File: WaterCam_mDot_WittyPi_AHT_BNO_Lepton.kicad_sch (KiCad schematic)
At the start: 9 parts, among them J1 GPIO, J2 FLIR Lepton Socket, J6 Witty Pi 4 7-Pin Header, Q1 NMOS

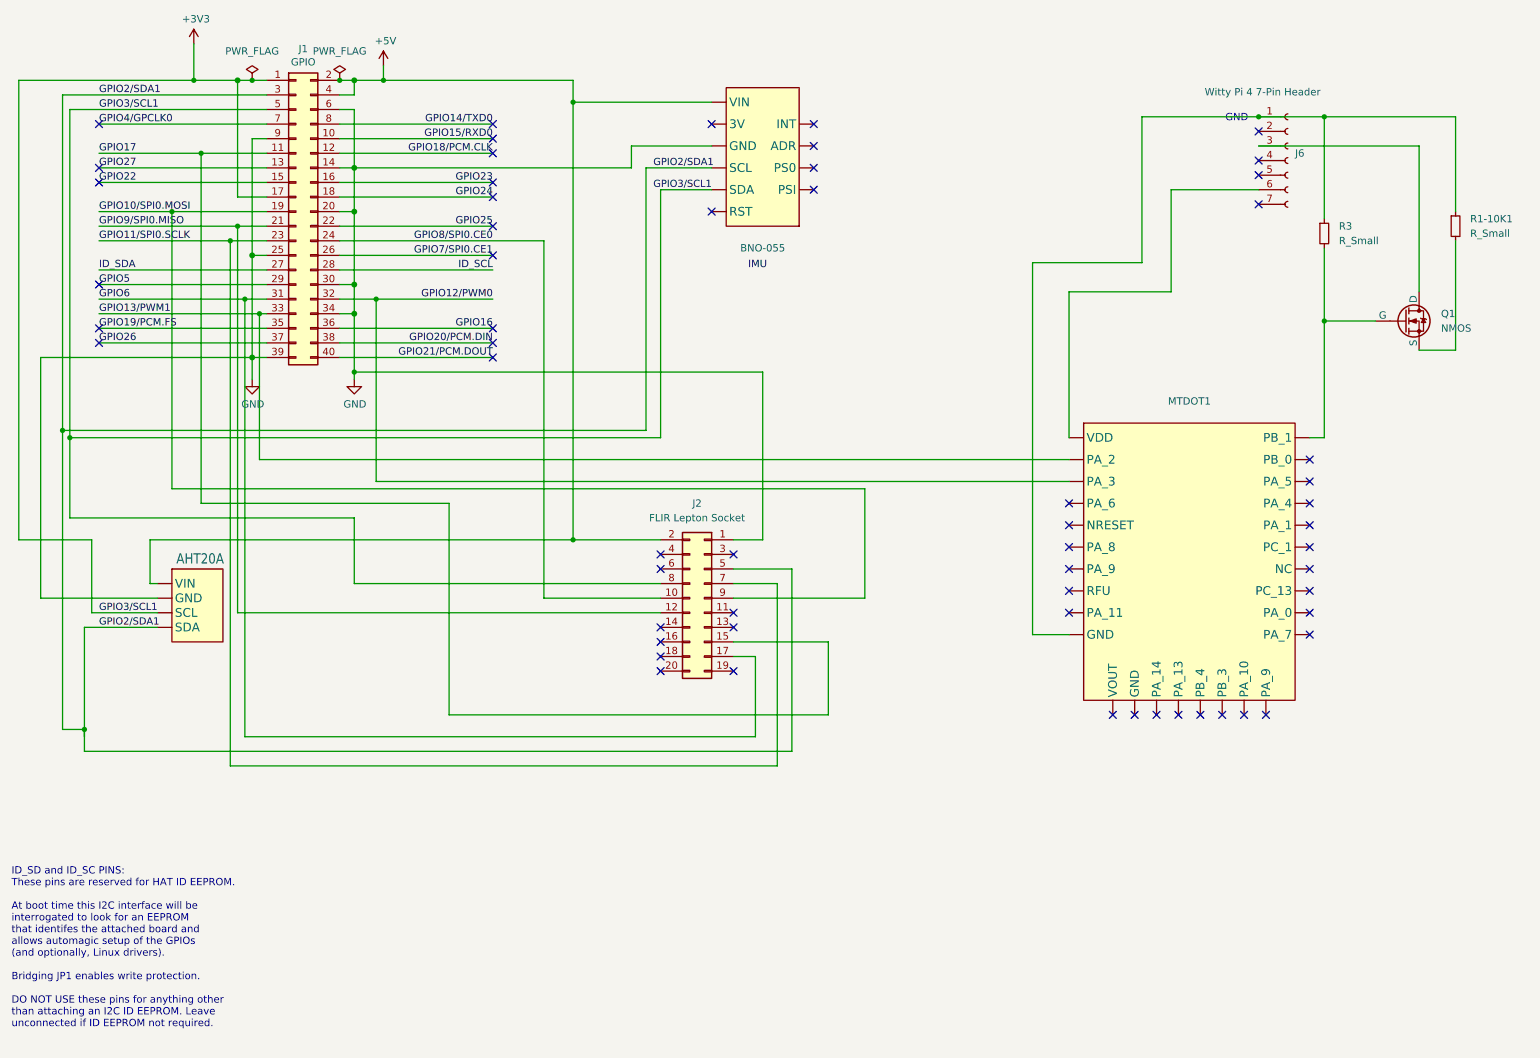
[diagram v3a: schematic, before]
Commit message: Add initial WaterCam PCB design integrating FLIR Lepton, BNO055, mDot, and Witty Pi 4
- Added schematic and PCB layout for 2-layer board in KiCad
- Integrated custom symbols and footprints (FLIR Lepton, mDot, Witty Pi 4)
- Included FFC slot for AWM 20624 15-pin ribbon cable
- Routed 5V and GND copper fills with thermal reliefs
- Verified design rule compliance (DRC clean)
- Project includes local symbol and footprint tables for portability
- Added README with fabrication and design documentation
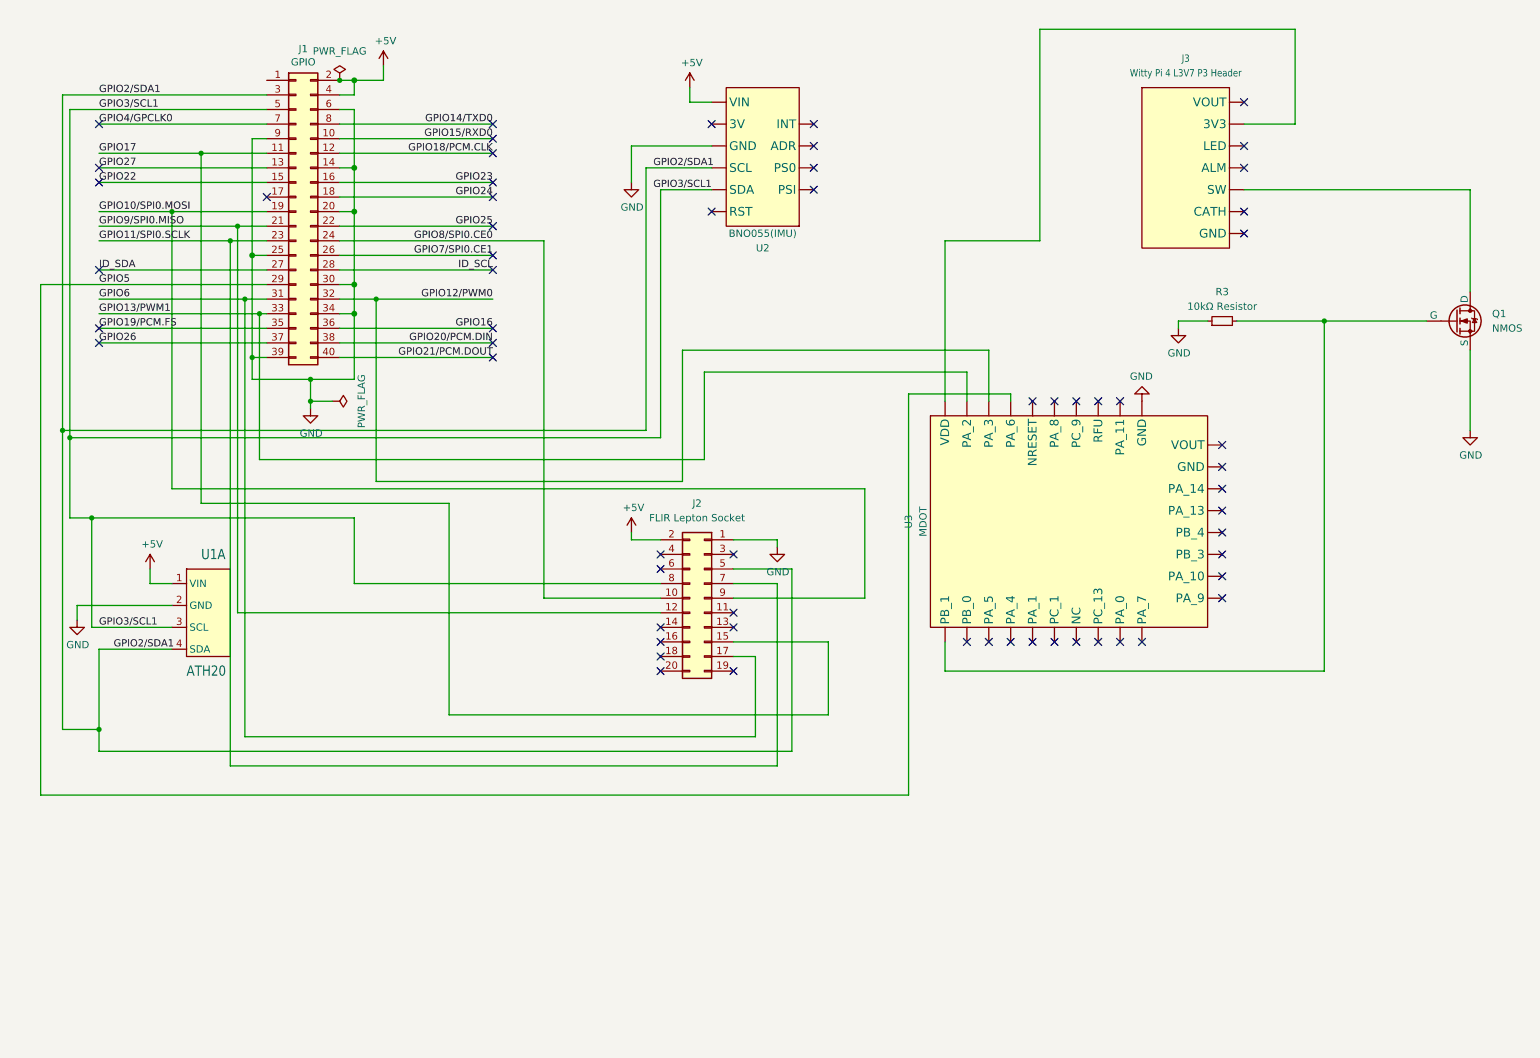
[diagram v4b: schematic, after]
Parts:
- removed J6: Witty Pi 4 7-Pin Header, Connector_PinSocket_2.54mm:PinSocket_1x07_P2.54mm_Vertical, symbol Connector:Conn_01x07_Socket
- removed R1-10K1: R_Small, Resistor_THT:R_Axial_DIN0207_L6.3mm_D2.5mm_P2.54mm_Vertical, symbol Device:R_Small
- added J3: Witty Pi 4 L3V7 P3 Header, Witty Pi 4:WittyPi4_Simple, symbol Adafruit BNO055 STEMMA QT-eagle-import:WittyPi4L3V7_P3Header
- J1: footprint Connector_PinSocket_2.54mm:PinSocket_2x20_P2.54mm_Vertical -> Raspberry Pi 4B 4GB:MODULE_RASPBERRY_PI_4B_4GB
- J2: footprint Connector_PinSocket_2.54mm:PinSocket_2x10_P2.54mm_Vertical -> FLIR Lepton:FLIR Lepton Breakout Board (Vertical)
- Q1: footprint (none) -> IRLB8721PBF Model:TO254P1067X483X2057-3
- R3: value R_Small -> 10kΩ Resistor
- U1: renamed from AHT20; value ~ -> ATH20; footprint Adafruit AHT20 Temperature & Humidity:JST_SH4 -> Adafruit AHT20 Temperature & Humidity:AHT20 Breakout Board
- U2: renamed from BNO-055; value ~ -> BNO055(IMU); footprint (none) -> Adafruit BNO055 STEMMA QT:BNO-055 Breakout
- U3: renamed from MTDOT1; value ~ -> MDOT; footprint (none) -> MDOT:MTDOT
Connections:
- net +5V: now also U1.1 (VIN), U2.6 (VIN); no longer U1. (SDA), U2. (VIN)
- net GND: now also Q1.3 (S), R3.1, U1.2 (GND), U2.4 (GND), U3.10 (GND); no longer U1. (SDA), U2. (VIN)
- net GPIO12/PWM0: now also U3.3 (PA_3); no longer U3. (PA_7)
- net GPIO13/PWM1: now also U3.2 (PA_2); no longer U3. (PA_7)
- net GPIO2/SDA1: now also U1.4 (SDA), U2.3 (SCL); no longer U1. (SDA), U2. (VIN)
- net GPIO5: now also U3.4 (PA_6)
- net at Q1.1 (D): now also J3.5 (SW)
- net at Q1.2 (G), R3.2: now also U3.19 (PB_1); no longer U3. (PA_7)
- removed net +3V3: J1.1 (Pin_1), J1.17 (Pin_17), J1.5 (Pin_5), J2.8 (Pin_8), U1. (SDA), U2. (VIN)
- new net: J3.2 (3V3), U3.1 (VDD)
- new net GPIO3/SCL1: J1.5 (Pin_5), J2.8 (Pin_8), U1.3 (SCL), U2.2 (SDA)
- no-connect marks 59 -> 61
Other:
- note removed: "GND"
- note removed: "ID_SD and ID_SC PINS: These pins are reserved for HAT ID EEPROM. At boot time this I2C interface will be interrogated to look for an EEPROM that identifes the attached board and allows automagic setup of the GPIOs (and optionally, Linux drivers). Bridging JP1 enables write protection. DO NOT USE these pins for anything other than attaching an I2C ID EEPROM. Leave unconnected if ID EEPROM not requ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"
- moved on the sheet: Q1, R3, U3

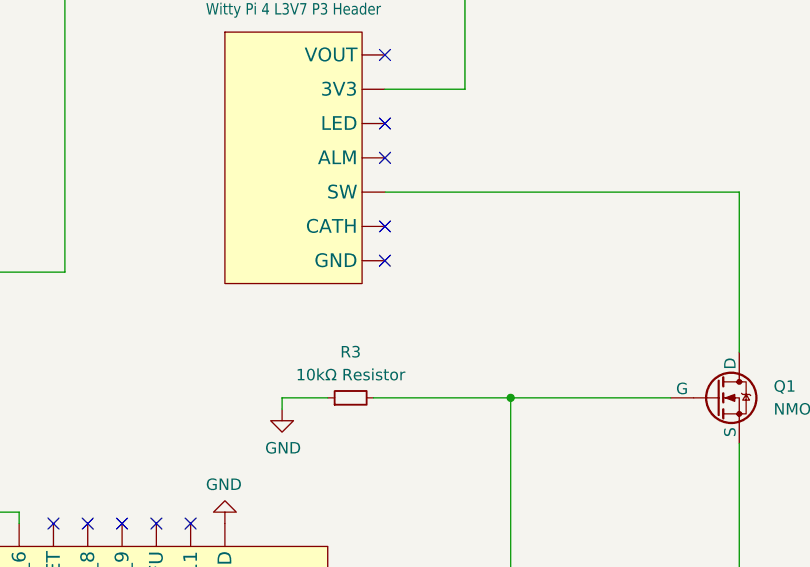
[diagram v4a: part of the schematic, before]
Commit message: Refine PCB power and ground layout for improved integrity and manufacturability
- Localized 5V plane to FLIR and IMU region to reduce EMI and isolate power
- Maintained full-board GND plane on bottom layer for low-impedance return paths
- Verified through-hole pad connections to both copper layers
- Removed unnecessary global power fills to prevent noise injection
- Cleaned up trace routing and ensured adequate spacing from board edges
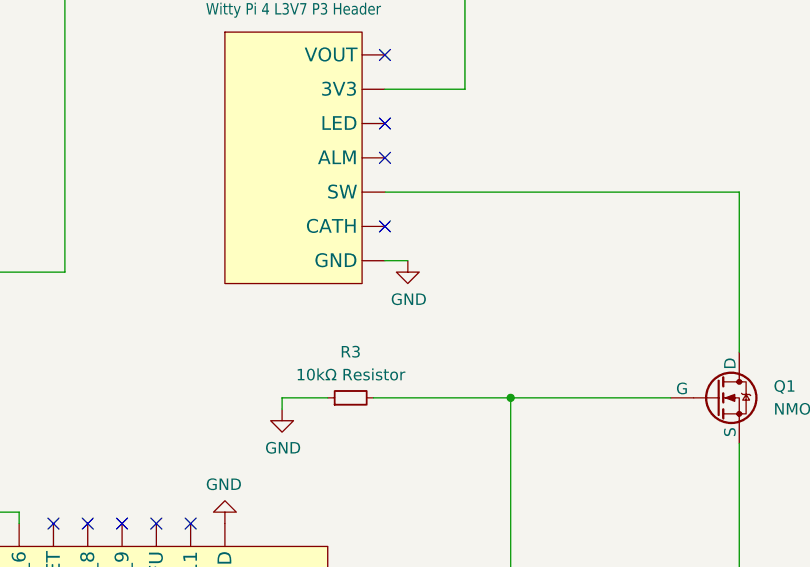
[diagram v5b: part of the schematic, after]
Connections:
- net GND: now also J3.7 (GND)
- no-connect marks 61 -> 60
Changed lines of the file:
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@@
-	)
-	(no_connect
-		(at 231.14 54.61)
 	)
 	(no_connect
@@
 		(pts
 			(xy 149.86 115.57) (xy 149.86 147.32)
+		)
+		(stroke
+			(width 0)
+			(type default)
+		)
+	)
+	(wire
+		(pts
+			(xy 233.68 54.61) (xy 231.14 54.61)
 		)
 		(stroke
@@
 					(unit 1)
 				)
+			)
+		)
+	)
+	(symbol
+		(lib_id "power:GND")
+		(at 233.68 54.61 0)
+		(unit 1)
+		(exclude_from_sim no)
+		(in_bom yes)
+		(on_board yes)
+		(dnp no)
+		(property "Reference" "#PWR04"
+			(at 233.68 60.96 0)
+			(effects
+				(font
+					(size 1.27 1.27)
+				)
+				(hide yes)
+			)
+		)
+		(property "Value" "GND"
+			(at 233.7943 58.9344 0)
+			(effects
+				(font
+					(size 1.27 1.27)
+				)
+			)
+		)
+		(property "Footprint" ""
+			(at 233.68 54.61 0)
+			(effects
+				(font
+					(size 1.27 1.27)
+				)
+			)
+		)
+		(property "Datasheet" ""
+			(at 233.68 54.61 0)
+			(effects
+				(font
+					(size 1.27 1.27)
+				)
+			)
+		)
+		(property "Description" ""
+			(at 233.68 54.61 0)
+			(effects
+				(font
+					(size 1.27 1.27)
+				)
+				(hide yes)
+			)
+		)
+		(pin "1"
+		)
+		(instances
+			(project "WaterCam_mDot_WittyPi_AHT_BNO_Lepton"
+				(path "/e63e39d7-6ac0-4ffd-8aa3-1841a4541b55"
+					(reference "#PWR04")
+					(unit 1)
+				)

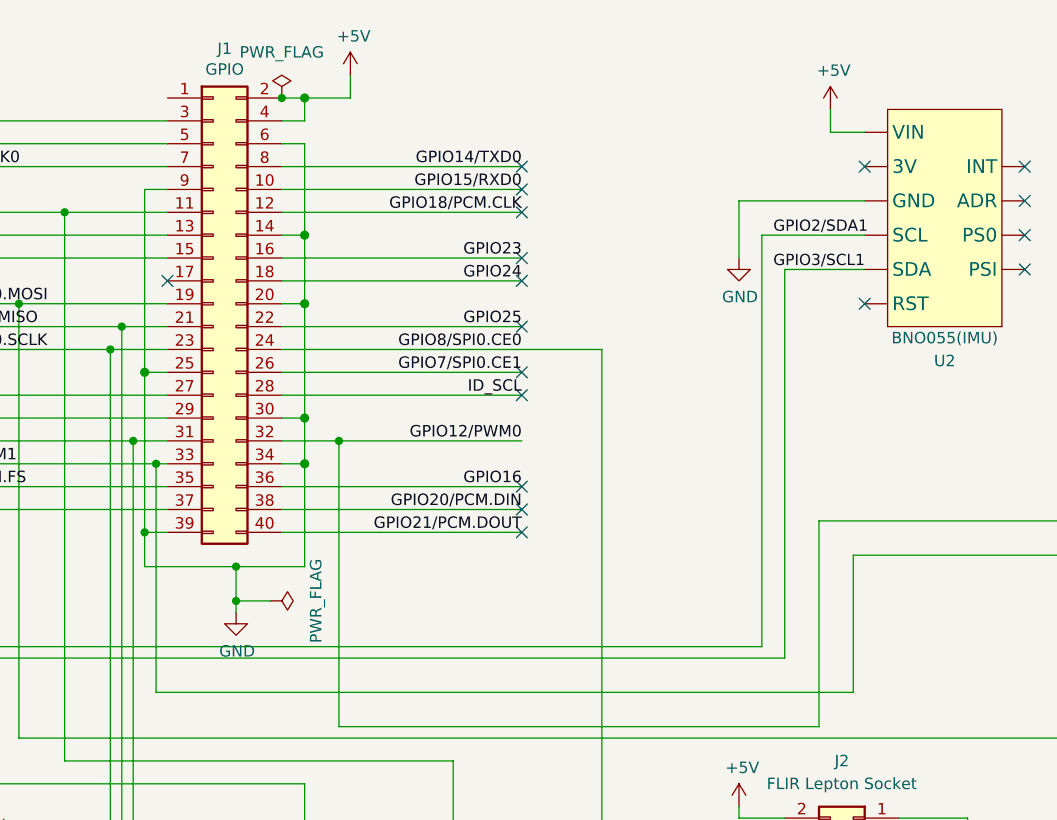
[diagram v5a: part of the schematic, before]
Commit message: Refactor silkscreen, component labels, and routing to align with Raspberry Pi and improve power integrity
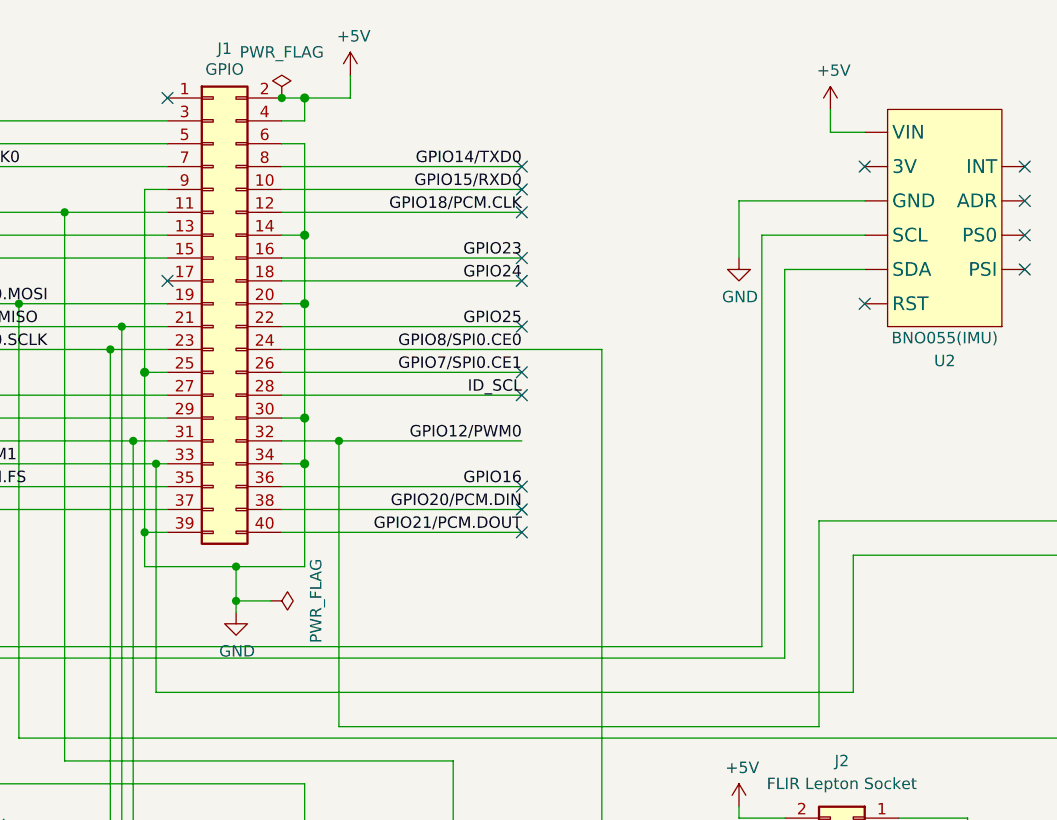
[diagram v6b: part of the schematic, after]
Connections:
- no-connect marks 60 -> 61
